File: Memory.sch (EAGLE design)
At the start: 7 parts, among them IC1 AT28C256ZIF, IC2 HM62256DIP

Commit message: Fix memory mapping issues
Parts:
- removed V2: 74HC00N, 74ttl-din:74HC00N
- added IC3: 74LS139N, 74xx-eu:74LS139N
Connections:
- removed net N$9: IC2.!CE, V2/1.Y
- new net N$1: IC2.!CE, IC3A.Y2
- net !MREQ: now also IC3A.A; no longer V2/1.A, V2/3.B
- net A15: now also IC3A.B; no longer V2/1.B, V2/2.A, V2/2.B, V2/2.Y, V2/3.A
- net GND: now also IC3A.G, IC3P.GND; no longer V2/-UB.-UB
- net N$2: now also IC3A.Y0; no longer V2/3.Y
- net VCC: now also IC3P.VCC; no longer V2/+UB.+UB
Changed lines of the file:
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@@
 <part name="P+3" library="supply1" deviceset="VCC" device=""/>
 <part name="GND3" library="supply1" deviceset="GND" device=""/>
-<part name="V2" library="74ttl-din" deviceset="74*00" device="N" technology="HC">
-<attribute name="MF" value="TEXAS INSTRUMENTS"/>
-<attribute name="MPN" value="SN74HC00N"/>
-<attribute name="OC_FARNELL" value="9590889"/>
-</part>
 <part name="IC2" library="jean" deviceset="HM62256" device="DIP">
 <attribute name="MF" value=""/>
@@
 <part name="P+6" library="supply1" deviceset="VCC" device=""/>
 <part name="GND5" library="supply1" deviceset="GND" device=""/>
+<part name="IC3" library="74xx-eu" deviceset="74*139" device="N" technology="LS"/>
+<part name="GND7" library="supply1" deviceset="GND" device=""/>
 </parts>
 <sheets>
@@
 <instance part="P+5" gate="VCC" x="63.5" y="114.3"/>
 <instance part="GND6" gate="1" x="33.02" y="109.22"/>
-<instance part="V2" gate="/1" x="73.66" y="187.96"/>
 <instance part="IC1" gate="G$1" x="129.54" y="114.3"/>
 <instance part="JP1" gate="A" x="-68.58" y="137.16" rot="R180"/>
-<instance part="V2" gate="/2" x="78.74" y="124.46"/>
-<instance part="V2" gate="/3" x="86.36" y="99.06"/>
 <instance part="GND4" gate="1" x="-83.82" y="162.56"/>
 <instance part="P+1" gate="VCC" x="-78.74" y="177.8"/>
-<instance part="V2" gate="/+UB" x="-78.74" y="167.64"/>
-<instance part="V2" gate="/-UB" x="-86.36" y="167.64"/>
 <instance part="C1" gate="G$1" x="25.4" y="104.14"/>
 <instance part="P+2" gate="VCC" x="25.4" y="109.22"/>
@@
 <instance part="P+6" gate="VCC" x="76.2" y="218.44"/>
 <instance part="GND5" gate="1" x="76.2" y="205.74"/>
+<instance part="IC3" gate="A" x="12.7" y="190.5"/>
+<instance part="GND7" gate="1" x="0" y="182.88"/>
+<instance part="IC3" gate="P" x="-104.14" y="172.72"/>
 </instances>
 <busses>
@@
 <wire x1="33.02" y1="167.64" x2="33.02" y2="185.42" width="0.1524" layer="91"/>
 <label x="33.02" y="185.42" size="1.778" layer="95"/>
-<pinref part="V2" gate="/1" pin="B"/>
-<wire x1="33.02" y1="185.42" x2="63.5" y2="185.42" width="0.1524" layer="91"/>
-</segment>
-<segment>
-<wire x1="73.66" y1="109.22" x2="73.66" y2="101.6" width="0.1524" layer="91"/>
-<wire x1="73.66" y1="101.6" x2="76.2" y2="101.6" width="0.1524" layer="91"/>
-<wire x1="88.9" y1="109.22" x2="73.66" y2="109.22" width="0.1524" layer="91"/>
-<label x="73.66" y="104.14" size="1.778" layer="95"/>
-<pinref part="V2" gate="/3" pin="A"/>
-<pinref part="V2" gate="/2" pin="Y"/>
-<wire x1="88.9" y1="124.46" x2="88.9" y2="109.22" width="0.1524" layer="91"/>
 </segment>
 <segment>
@@
 <segment>
 <wire x1="76.2" y1="167.64" x2="73.66" y2="167.64" width="0.1524" layer="91"/>
-<wire x1="73.66" y1="167.64" x2="73.66" y2="132.08" width="0.1524" layer="91"/>
-<wire x1="73.66" y1="132.08" x2="68.58" y2="132.08" width="0.1524" layer="91"/>
-<pinref part="V2" gate="/2" pin="A"/>
-<wire x1="68.58" y1="132.08" x2="68.58" y2="127" width="0.1524" layer="91"/>
-<pinref part="V2" gate="/2" pin="B"/>
-<wire x1="68.58" y1="127" x2="68.58" y2="121.92" width="0.1524" layer="91"/>
-<junction x="68.58" y="127"/>
+</segment>
+<segment>
+<wire x1="-2.54" y1="167.64" x2="-5.08" y2="167.64" width="0.1524" layer="91"/>
+<wire x1="-5.08" y1="167.64" x2="-5.08" y2="190.5" width="0.1524" layer="91"/>
+<pinref part="IC3" gate="A" pin="B"/>
+<wire x1="-5.08" y1="190.5" x2="0" y2="190.5" width="0.1524" layer="91"/>
 </segment>
 </net>
@@
 <pinref part="P+1" gate="VCC" pin="VCC"/>
 <wire x1="-66.04" y1="170.18" x2="-78.74" y2="170.18" width="0.1524" layer="91"/>
-<pinref part="V2" gate="/+UB" pin="+UB"/>
-<wire x1="-78.74" y1="170.18" x2="-78.74" y2="175.26" width="0.1524" layer="91"/>
-<junction x="-78.74" y="170.18"/>
+<wire x1="-78.74" y1="170.18" x2="-78.74" y2="172.72" width="0.1524" layer="91"/>
+<pinref part="IC3" gate="P" pin="VCC"/>
+<wire x1="-78.74" y1="172.72" x2="-78.74" y2="175.26" width="0.1524" layer="91"/>
+<wire x1="-104.14" y1="180.34" x2="-81.28" y2="180.34" width="0.1524" layer="91"/>
+<wire x1="-81.28" y1="180.34" x2="-81.28" y2="172.72" width="0.1524" layer="91"/>
+<wire x1="-81.28" y1="172.72" x2="-78.74" y2="172.72" width="0.1524" layer="91"/>
+<junction x="-78.74" y="172.72"/>
 </segment>
 <segment>
@@
 <pinref part="GND4" gate="1" pin="GND"/>
 <wire x1="-66.04" y1="167.64" x2="-83.82" y2="165.1" width="0.1524" layer="91"/>
-<wire x1="-83.82" y1="165.1" x2="-86.36" y2="165.1" width="0.1524" layer="91"/>
 <junction x="-83.82" y="165.1"/>
-<wire x1="-86.36" y1="165.1" x2="-88.9" y2="165.1" width="0.1524" layer="91"/>
+<wire x1="-83.82" y1="165.1" x2="-88.9" y2="165.1" width="0.1524" layer="91"/>
 <wire x1="-88.9" y1="165.1" x2="-88.9" y2="205.74" width="0.1524" layer="91"/>
 <pinref part="JP1" gate="A" pin="GND@2"/>
 <wire x1="-88.9" y1="205.74" x2="-66.04" y2="205.74" width="0.1524" layer="91"/>
-<pinref part="V2" gate="/-UB" pin="-UB"/>
-<junction x="-86.36" y="165.1"/>
+<pinref part="IC3" gate="P" pin="GND"/>
+<wire x1="-104.14" y1="165.1" x2="-88.9" y2="165.1" width="0.1524" layer="91"/>
+<junction x="-88.9" y="165.1"/>
 </segment>
 <segment>
@@
 <pinref part="GND5" gate="1" pin="GND"/>
 </segment>
+<segment>
+<pinref part="IC3" gate="A" pin="G"/>
+<pinref part="GND7" gate="1" pin="GND"/>
+</segment>
 </net>
 <net name="!MREQ" class="0">
 <segment>
-<wire x1="-48.26" y1="198.12" x2="58.42" y2="198.12" width="0.1524" layer="91"/>
-<pinref part="V2" gate="/1" pin="A"/>
-<wire x1="63.5" y1="190.5" x2="58.42" y2="190.5" width="0.1524" layer="91"/>
-<wire x1="58.42" y1="190.5" x2="58.42" y2="198.12" width="0.1524" layer="91"/>
-<wire x1="58.42" y1="198.12" x2="91.44" y2="198.12" width="0.1524" layer="91"/>
-<wire x1="91.44" y1="198.12" x2="91.44" y2="114.3" width="0.1524" layer="91"/>
-<junction x="58.42" y="198.12"/>
-<wire x1="91.44" y1="114.3" x2="71.12" y2="114.3" width="0.1524" layer="91"/>
-<wire x1="71.12" y1="114.3" x2="71.12" y2="96.52" width="0.1524" layer="91"/>
-<wire x1="71.12" y1="96.52" x2="76.2" y2="96.52" width="0.1524" layer="91"/>
-<label x="71.12" y="93.98" size="1.778" layer="95"/>
-<label x="60.96" y="193.04" size="1.778" layer="95"/>
+<wire x1="-48.26" y1="198.12" x2="-5.08" y2="198.12" width="0.1524" layer="91"/>
+<wire x1="-5.08" y1="198.12" x2="91.44" y2="198.12" width="0.1524" layer="91"/>
 <wire x1="-48.26" y1="198.12" x2="-48.26" y2="182.88" width="0.1524" layer="91"/>
 <pinref part="JP1" gate="A" pin="!MREQ"/>
 <wire x1="-48.26" y1="182.88" x2="-66.04" y2="182.88" width="0.1524" layer="91"/>
-<pinref part="V2" gate="/3" pin="B"/>
-</segment>
-</net>
-<net name="N$9" class="0">
-<segment>
-<pinref part="IC2" gate="G$1" pin="!CE"/>
-<pinref part="V2" gate="/1" pin="Y"/>
-<wire x1="86.36" y1="147.32" x2="60.96" y2="147.32" width="0.1524" layer="91"/>
-<wire x1="83.82" y1="187.96" x2="86.36" y2="187.96" width="0.1524" layer="91"/>
-<wire x1="86.36" y1="187.96" x2="86.36" y2="147.32" width="0.1524" layer="91"/>
+<pinref part="IC3" gate="A" pin="A"/>
+<wire x1="0" y1="193.04" x2="-5.08" y2="193.04" width="0.1524" layer="91"/>
+<wire x1="-5.08" y1="193.04" x2="-5.08" y2="198.12" width="0.1524" layer="91"/>
+<junction x="-5.08" y="198.12"/>
 </segment>
 </net>
@@
 <net name="N$2" class="0">
 <segment>
-<wire x1="96.52" y1="99.06" x2="99.06" y2="99.06" width="0.1524" layer="91"/>
-<wire x1="99.06" y1="99.06" x2="99.06" y2="101.6" width="0.1524" layer="91"/>
 <pinref part="IC1" gate="G$1" pin="!CE"/>
 <wire x1="99.06" y1="101.6" x2="114.3" y2="101.6" width="0.1524" layer="91"/>
-<pinref part="V2" gate="/3" pin="Y"/>
-</segment>
-</net>
+<pinref part="IC3" gate="A" pin="Y0"/>
+<wire x1="25.4" y1="193.04" x2="99.06" y2="193.04" width="0.1524" layer="91"/>
+<wire x1="99.06" y1="193.04" x2="99.06" y2="101.6" width="0.1524" layer="91"/>
+</segment>
+</net>
+<net name="N$1" class="0">
+<segment>
+<pinref part="IC3" gate="A" pin="Y2"/>
+<wire x1="25.4" y1="187.96" x2="73.66" y2="187.96" width="0.1524" layer="91"/>
+<wire x1="73.66" y1="187.96" x2="73.66" y2="147.32" width="0.1524" layer="91"/>
+<pinref part="IC2" gate="G$1" pin="!CE"/>
+<wire x1="73.66" y1="147.32" x2="60.96" y2="147.32" width="0.1524" layer="91"/>
+</segment>
+</net>

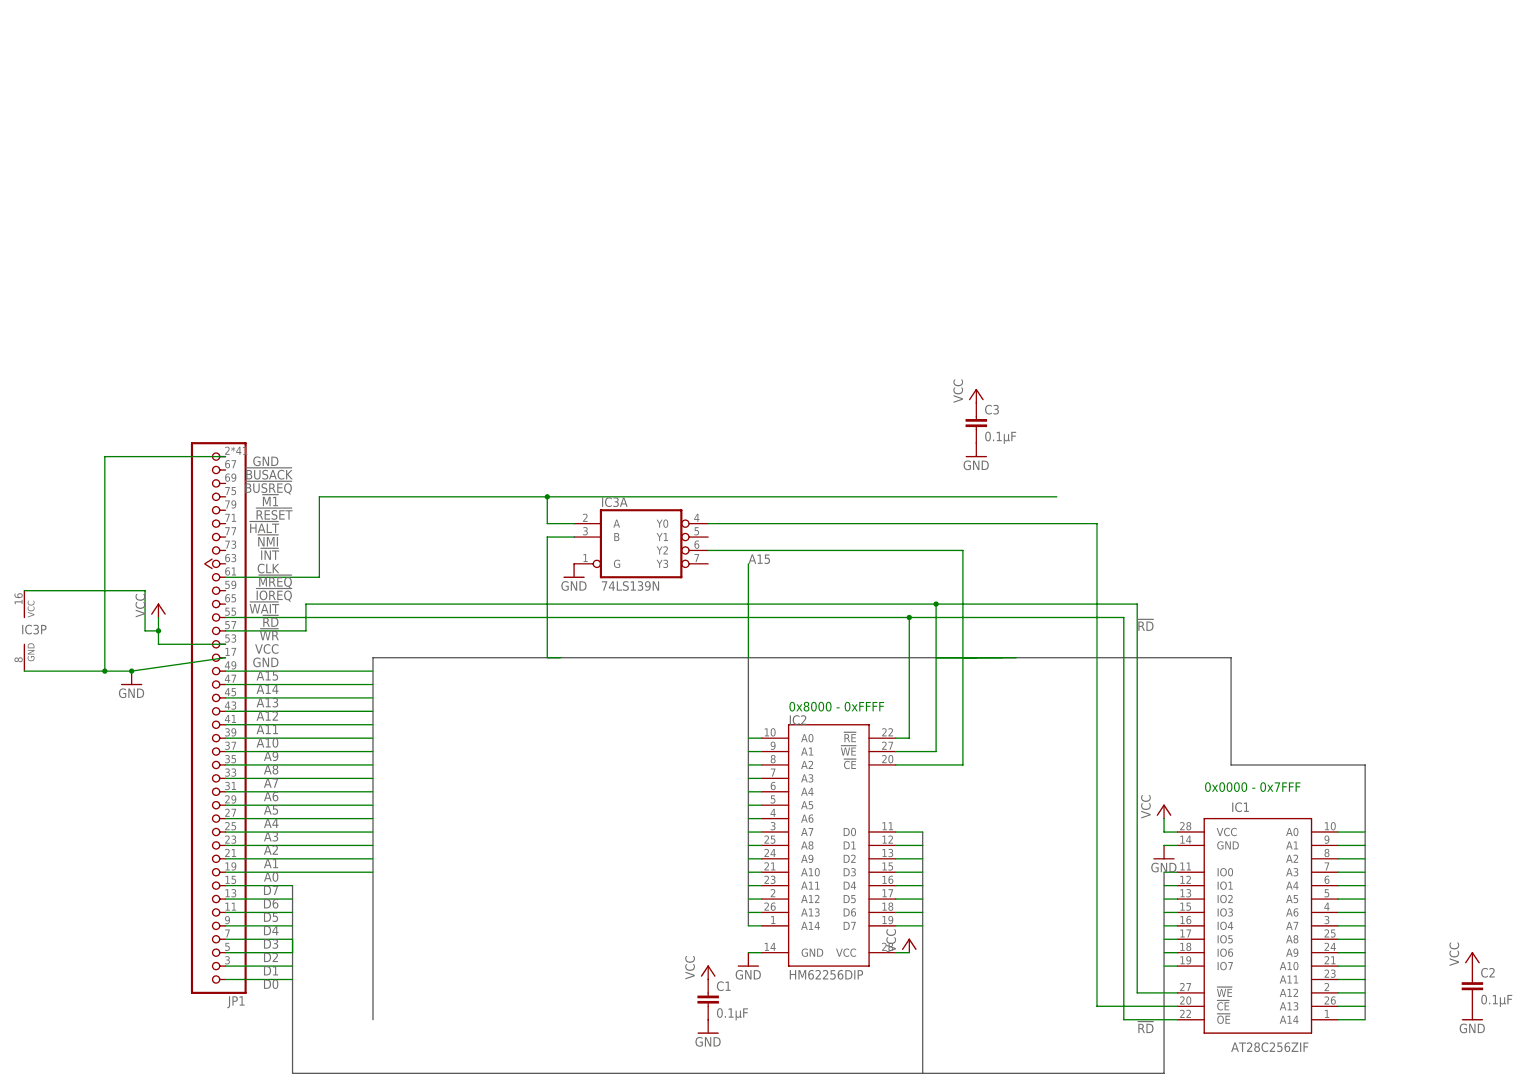
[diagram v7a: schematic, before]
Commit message: Added memory ram banking to the memory board
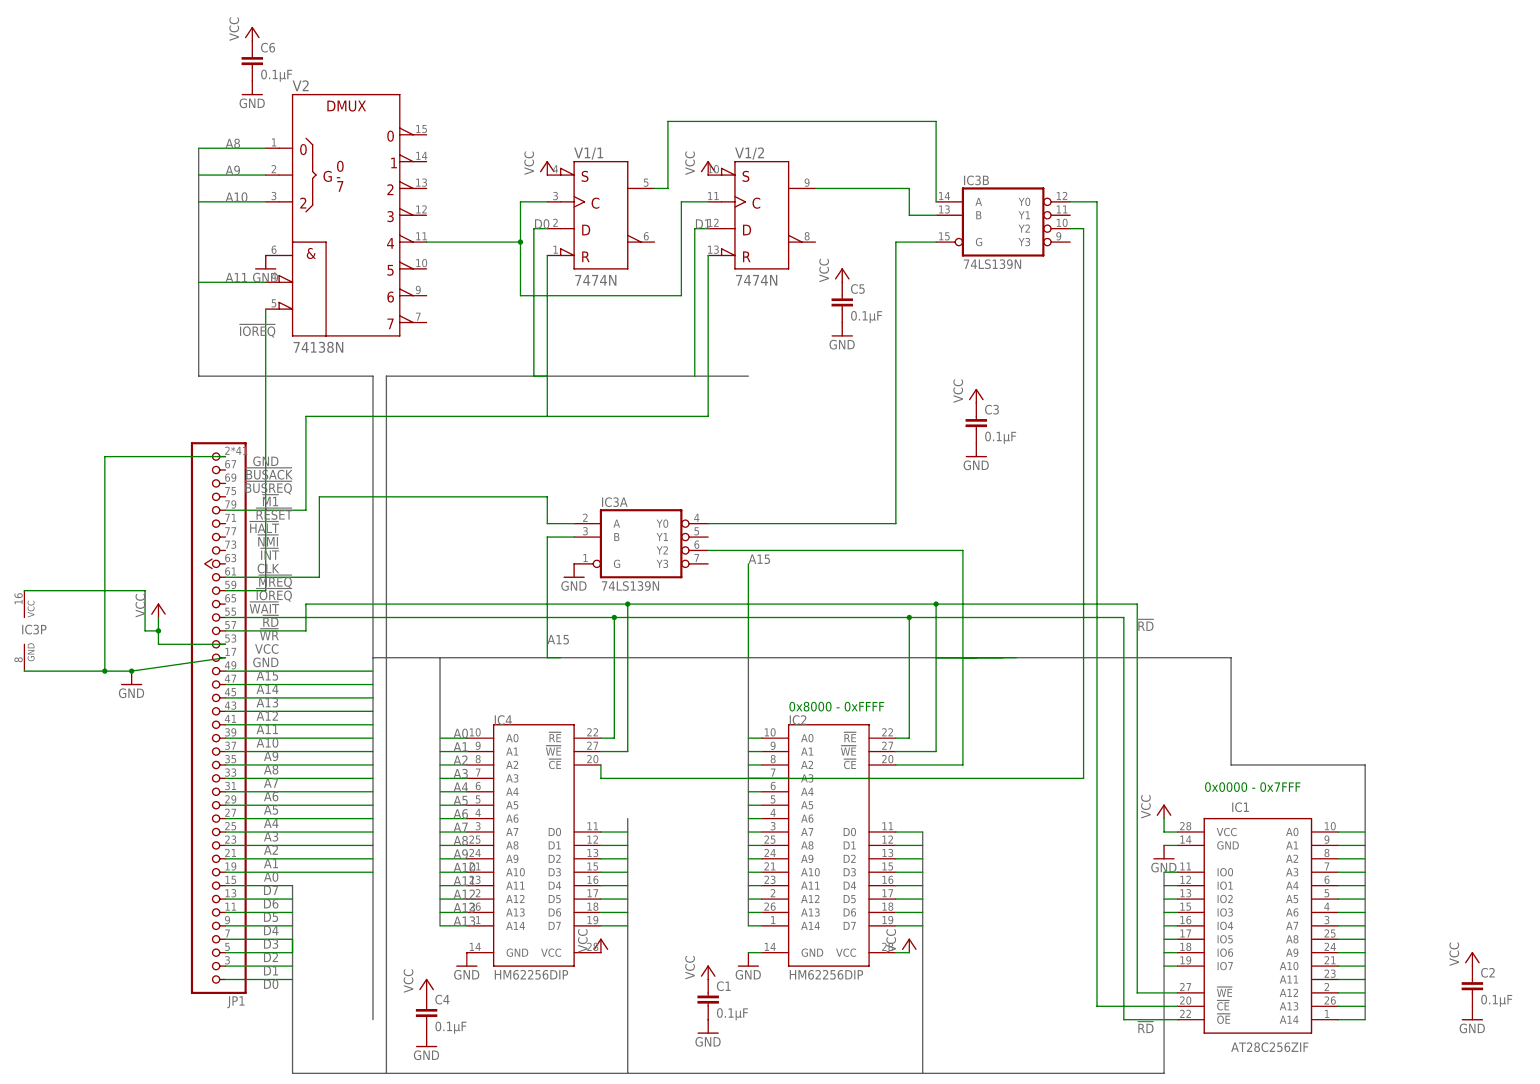
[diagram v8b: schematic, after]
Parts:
- added C4, C5, C6: 0.1µF, capacitor-wima:C5/2.5
- added IC4: HM62256DIP, jean:HM62256DIP
- added V1: 7474N, 74ttl-din:7474N
- added V2: 74138N, 74ttl-din:74138N
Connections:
- new net !IOREQ: JP1.!IOREQ, V21.!G2B
- new net N$3: IC3B.A, V1/1.Q
- new net N$4: V1/1.CLK, V1/2.CLK, V21.Y4
- new net N$5: IC3B.B, V1/2.Q
- new net N$6: JP1.!RESET, V1/1.!CLR, V1/2.!CLR
- new net N$7: IC3A.Y0, IC3B.G
- new net N$9: IC3B.Y2, IC4.!CE
- net !RD: now also IC4.!RE
- net !WR: now also IC4.!WE
- net A0: now also IC4.A0
- net A1: now also IC4.A1
- net A10: now also IC4.A10, V21.C
- net A11: now also IC4.A11, V21.!G2A
- net A12: now also IC4.A12
- net A13: now also IC4.A13
- net A14: now also IC4.A14
- net A2: now also IC4.A2
- net A3: now also IC4.A3
- net A4: now also IC4.A4
- net A5: now also IC4.A5
- net A6: now also IC4.A6
- net A7: now also IC4.A7
- net A8: now also IC4.A8, V21.A
- net A9: now also IC4.A9, V21.B
- net D0: now also IC4.D0, V1/1.D
- net D1: now also IC4.D1, V1/2.D
- net D2: now also IC4.D2
- net D3: now also IC4.D3
- net D4: now also IC4.D4
- net D5: now also IC4.D5
- net D6: now also IC4.D6
- net D7: now also IC4.D7
- net GND: now also C4.2, C5.2, C6.2, IC4.GND, V21.G1
- net N$2: now also IC3B.Y0; no longer IC3A.Y0
- net VCC: now also C4.1, C5.1, C6.1, IC4.VCC, V1/1.!PRE, V1/2.!PRE
